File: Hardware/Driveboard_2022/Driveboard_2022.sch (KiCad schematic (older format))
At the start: 60 parts, among them SW1 SW_Push, SW2 SW_Push, SW3 SW_Push, SW4 SW_SPST, SW5 SW_Push, SW6 SW_Push, SW7 SW_Push, U1 OKI 3V3, U2 Teensy4.1_DEV-16771

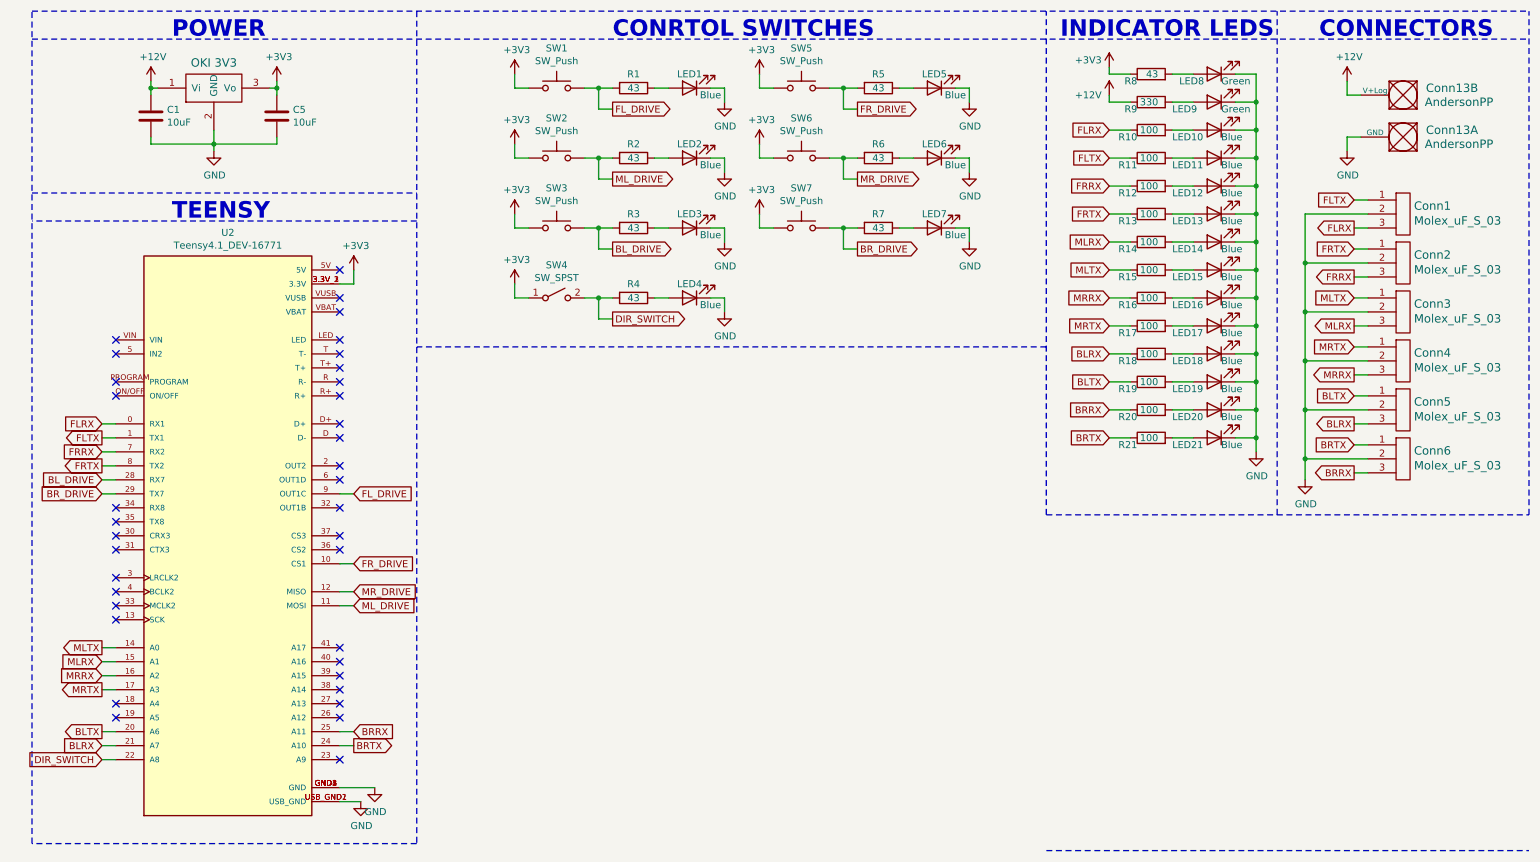
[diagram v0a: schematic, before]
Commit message: Fixed Ethernet Port
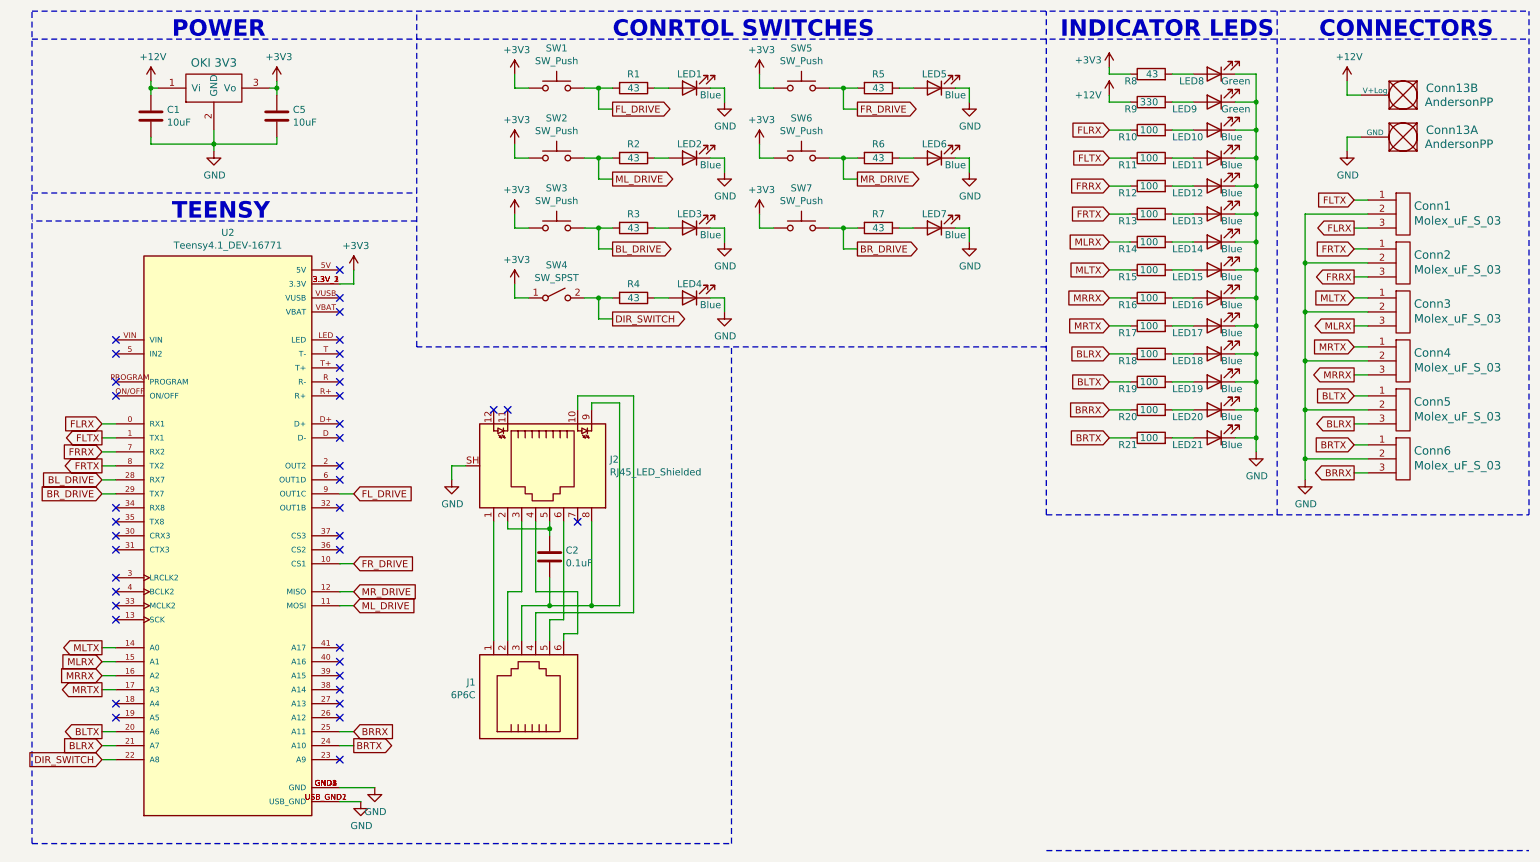
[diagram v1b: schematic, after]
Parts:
- added C2: 0.1uF, Capacitor_SMD:C_0603_1608Metric_Pad1.08x0.95mm_HandSolder, symbol Device:C
- added J1: 6P6C, Connector_PinHeader_2.00mm:PinHeader_2x03_P2.00mm_Vertical, symbol Connector:6P6C
- added J2: RJ45_LED_Shielded, MRDT_Connectors:RJ45_Teensy, symbol Connector:RJ45_LED_Shielded
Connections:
- net GND: now also J2.SH
- new net: J1.1, J2.1
- new net: J1.4, J2.10
- new net: C2.1, J2.2, J2.5
- new net: J1.2, J2.3
- new net: J1.6, J2.4
- new net: J1.5, J2.6
- new net: C2.2, J1.3, J2.8, J2.9
- no-connect marks 36 -> 39
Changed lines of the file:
@@
 CONNECTORS
-Wire Notes Line
-	3250 500  3250 6450
 Wire Notes Line
 	500  6450 500  500
@@
 Wire Notes Line
 	3250 2000 500  2000
-Wire Notes Line
-	3250 6450 500  6450
 $Comp
 L power:GND #PWR020
@@
 NoConn ~ 1100 5450
 NoConn ~ 1100 5550
+$Comp
+L Connector:6P6C J1
+U 1 1 62137B17
+P 4000 5400
+F 0 "J1" V 4103 5070 50  0000 R CNN
+F 1 "6P6C" V 4012 5070 50  0000 R CNN
+F 2 "Connector_PinHeader_2.00mm:PinHeader_2x03_P2.00mm_Vertical" V 4000 5425 50  0001 C CNN
+F 3 "~" V 4000 5425 50  0001 C CNN
+	1    4000 5400
+	0    1    -1   0
+$EndComp
+$Comp
+L power:GND #PWR02
+U 1 1 62152008
+P 3500 3850
+F 0 "#PWR02" H 3500 3600 50  0001 C CNN
+F 1 "GND" H 3505 3677 50  0000 C CNN
+F 2 "" H 3500 3850 50  0001 C CNN
+F 3 "" H 3500 3850 50  0001 C CNN
+	1    3500 3850
+	1    0    0    -1
+$EndComp
+Wire Wire Line
+	3500 3850 3500 3750
+Wire Wire Line
+	3500 3750 3600 3750
+Wire Wire Line
+	4200 4250 4200 4200
+Wire Wire Line
+	4200 4200 3900 4200
+Wire Wire Line
+	3900 4200 3900 4150
+Connection ~ 4200 4200
+Wire Wire Line
+	4200 4200 4200 4150
+Wire Wire Line
+	4200 4550 4200 4750
+Wire Wire Line
+	4500 4150 4500 4750
+Wire Wire Line
+	4500 4750 4200 4750
+Wire Wire Line
+	4500 3350 4500 3300
+Wire Wire Line
+	4500 3300 4700 3300
+Wire Wire Line
+	4400 3350 4400 3250
+Wire Wire Line
+	4400 3250 4800 3250
+NoConn ~ 3800 3350
+NoConn ~ 3900 3350
+Wire Wire Line
+	3800 4150 3800 5000
+Wire Wire Line
+	4000 5000 4000 4750
+Wire Wire Line
+	4000 4750 4200 4750
+Connection ~ 4200 4750
+Wire Wire Line
+	4300 5000 4300 4950
+Wire Wire Line
+	4300 4950 4400 4950
+Wire Wire Line
+	4400 4950 4400 4650
+Wire Wire Line
+	4400 4650 4100 4650
+Wire Wire Line
+	4100 4650 4100 4150
+Wire Wire Line
+	4200 4850 4300 4850
+Wire Wire Line
+	4300 4850 4300 4150
+Wire Wire Line
+	4200 4850 4200 5000
+Wire Wire Line
+	4100 5000 4100 4800
+Wire Wire Line
+	4100 4800 4800 4800
+Wire Wire Line
+	4800 3250 4800 4800
+Wire Wire Line
+	4700 4750 4500 4750
+Wire Wire Line
+	4700 3300 4700 4750
+Connection ~ 4500 4750
+Wire Wire Line
+	3900 5000 3900 4650
+Wire Wire Line
+	3900 4650 4000 4650
+Wire Wire Line
+	4000 4650 4000 4150
+NoConn ~ 4400 4150
+$Comp
+L Connector:RJ45_LED_Shielded J2
+U 1 1 62134E16
+P 4100 3750
+F 0 "J2" V 4054 4280 50  0000 L CNN
+F 1 "RJ45_LED_Shielded" V 4145 4280 50  0000 L CNN
+F 2 "MRDT_Connectors:RJ45_Teensy" V 4100 3775 50  0001 C CNN
+F 3 "~" V 4100 3775 50  0001 C CNN
+	1    4100 3750
+	0    1    1    0
+$EndComp
+$Comp
+L Device:C C2
+U 1 1 621516A0
+P 4200 4400
+F 0 "C2" H 4315 4446 50  0000 L CNN
+F 1 "0.1uF" H 4315 4355 50  0000 L CNN
+F 2 "Capacitor_SMD:C_0603_1608Metric_Pad1.08x0.95mm_HandSolder" H 4238 4250 50  0001 C CNN
+F 3 "~" H 4200 4400 50  0001 C CNN
+	1    4200 4400
+	1    0    0    -1
+$EndComp
+Wire Notes Line
+	3250 2900 3250 500
+Wire Notes Line
+	5500 6450 5500 2900
+Wire Notes Line
+	500  6450 5500 6450
 $EndSCHEMATC

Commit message: Board Review Changes
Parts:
- R1, R2, R3, R4, R5, R6, R7, R8: value 43 -> 100
- R9: value 330 -> 1k
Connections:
- net DIR_SWITCH: now also U2.33 (MCLK2); no longer U2.22 (A8)
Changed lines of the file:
@@
 Wire Wire Line
 	1000 3850 1100 3850
-Text GLabel 1000 5850 0    50   Input ~ 0
+Text GLabel 1000 4750 0    50   Input ~ 0
 DIR_SWITCH
 Wire Wire Line
-	1000 5850 1100 5850
+	1000 4750 1100 4750
 $Comp
 L power:+12V #PWR01
@@
 P 4800 1050
 F 0 "R1" V 4700 1050 50  0000 C CNN
-F 1 "43" V 4800 1050 50  0000 C CNN
+F 1 "100" V 4800 1050 50  0000 C CNN
 F 2 "Resistor_SMD:R_0603_1608Metric_Pad0.98x0.95mm_HandSolder" V 4730 1050 50  0001 C CNN
 F 3 "~" H 4800 1050 50  0001 C CNN
@@
 P 4800 1550
 F 0 "R2" V 4700 1550 50  0000 C CNN
-F 1 "43" V 4800 1550 50  0000 C CNN
+F 1 "100" V 4800 1550 50  0000 C CNN
 F 2 "Resistor_SMD:R_0603_1608Metric_Pad0.98x0.95mm_HandSolder" V 4730 1550 50  0001 C CNN
 F 3 "~" H 4800 1550 50  0001 C CNN
@@
 P 4800 2050
 F 0 "R3" V 4700 2050 50  0000 C CNN
-F 1 "43" V 4800 2050 50  0000 C CNN
+F 1 "100" V 4800 2050 50  0000 C CNN
 F 2 "Resistor_SMD:R_0603_1608Metric_Pad0.98x0.95mm_HandSolder" V 4730 2050 50  0001 C CNN
 F 3 "~" H 4800 2050 50  0001 C CNN
@@
 P 6550 1050
 F 0 "R5" V 6450 1050 50  0000 C CNN
-F 1 "43" V 6550 1050 50  0000 C CNN
+F 1 "100" V 6550 1050 50  0000 C CNN
 F 2 "Resistor_SMD:R_0603_1608Metric_Pad0.98x0.95mm_HandSolder" V 6480 1050 50  0001 C CNN
 F 3 "~" H 6550 1050 50  0001 C CNN
@@
 P 6550 1550
 F 0 "R6" V 6450 1550 50  0000 C CNN
-F 1 "43" V 6550 1550 50  0000 C CNN
+F 1 "100" V 6550 1550 50  0000 C CNN
 F 2 "Resistor_SMD:R_0603_1608Metric_Pad0.98x0.95mm_HandSolder" V 6480 1550 50  0001 C CNN
 F 3 "~" H 6550 1550 50  0001 C CNN
@@
 P 6550 2050
 F 0 "R7" V 6450 2050 50  0000 C CNN
-F 1 "43" V 6550 2050 50  0000 C CNN
+F 1 "100" V 6550 2050 50  0000 C CNN
 F 2 "Resistor_SMD:R_0603_1608Metric_Pad0.98x0.95mm_HandSolder" V 6480 2050 50  0001 C CNN
 F 3 "~" H 6550 2050 50  0001 C CNN
@@
 P 4800 2550
 F 0 "R4" V 4700 2550 50  0000 C CNN
-F 1 "43" V 4800 2550 50  0000 C CNN
+F 1 "100" V 4800 2550 50  0000 C CNN
 F 2 "Resistor_SMD:R_0603_1608Metric_Pad0.98x0.95mm_HandSolder" V 4730 2550 50  0001 C CNN
 F 3 "~" H 4800 2550 50  0001 C CNN
@@
 P 8500 950
 F 0 "R8" V 8450 1050 50  0000 L CNN
-F 1 "43" V 8500 900 50  0000 L CNN
+F 1 "100" V 8500 900 50  0000 L CNN
 F 2 "Resistor_SMD:R_0603_1608Metric_Pad0.98x0.95mm_HandSolder" V 8430 950 50  0001 C CNN
 F 3 "~" H 8500 950 50  0001 C CNN
@@
 P 8500 1150
 F 0 "R9" V 8450 1250 50  0000 L CNN
-F 1 "330" V 8500 1100 50  0000 L CNN
+F 1 "1k" V 8500 1100 50  0000 L CNN
 F 2 "Resistor_SMD:R_0603_1608Metric_Pad0.98x0.95mm_HandSolder" V 8430 1150 50  0001 C CNN
 F 3 "~" H 8500 1150 50  0001 C CNN
@@
 NoConn ~ 2700 5850
 NoConn ~ 1100 4850
-NoConn ~ 1100 4750
 NoConn ~ 1100 4650
 NoConn ~ 1100 4550
@@
 Wire Notes Line
 	500  6450 5500 6450
+NoConn ~ 1100 5850
 $EndSCHEMATC

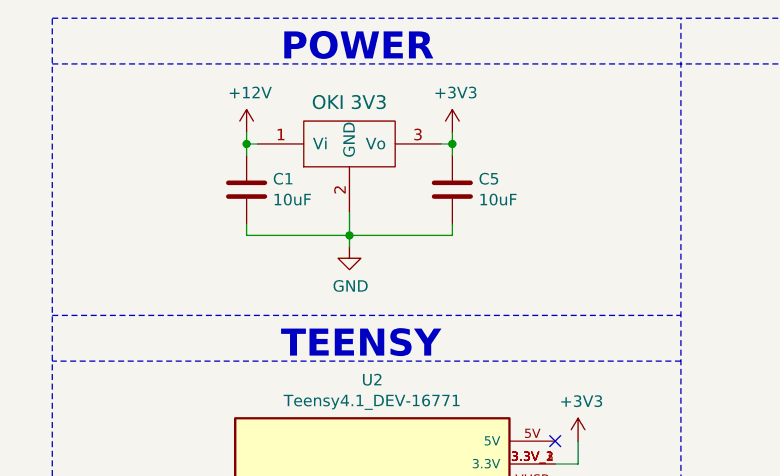
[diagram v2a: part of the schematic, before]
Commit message: Changed Buck Converter; Redid Gerbs
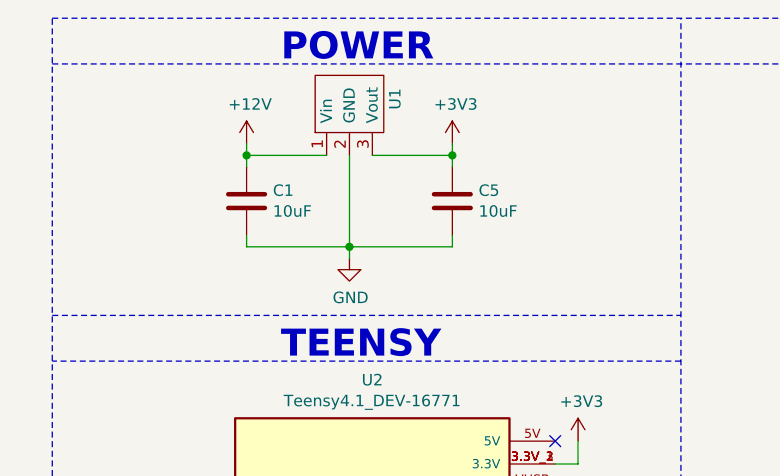
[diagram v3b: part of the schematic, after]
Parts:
- removed U1: OKI 3V3, MRDT_Devices:OKI_Horizontal, symbol MRDT_Devices:OKI
- added U1: TSR1-2433, MRDT_Devices:TSR_1-2433, symbol MRDT_Devices:TSR1-2433
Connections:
- net +12V: now also U1.1 (Vin)
- net +3V3: now also U1.3 (Vout)
- net GND: now also U1.2 (GND)
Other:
- moved on the sheet: C1, C5
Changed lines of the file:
@@
 L power:GND #PWR05
 U 1 1 614AB02E
-P 1800 1500
-F 0 "#PWR05" H 1800 1250 50  0001 C CNN
-F 1 "GND" H 1805 1327 50  0000 C CNN
-F 2 "" H 1800 1500 50  0001 C CNN
-F 3 "" H 1800 1500 50  0001 C CNN
-	1    1800 1500
+P 1800 1550
+F 0 "#PWR05" H 1800 1300 50  0001 C CNN
+F 1 "GND" H 1805 1377 50  0000 C CNN
+F 2 "" H 1800 1550 50  0001 C CNN
+F 3 "" H 1800 1550 50  0001 C CNN
+	1    1800 1550
 	1    0    0    -1
 $EndComp
@@
 L Device:C C1
 U 1 1 614B147D
-P 1350 1250
-F 0 "C1" H 1465 1296 50  0000 L CNN
-F 1 "10uF" H 1465 1205 50  0000 L CNN
-F 2 "Capacitor_SMD:C_0603_1608Metric_Pad1.08x0.95mm_HandSolder" H 1388 1100 50  0001 C CNN
-F 3 "~" H 1350 1250 50  0001 C CNN
-	1    1350 1250
+P 1350 1300
+F 0 "C1" H 1465 1346 50  0000 L CNN
+F 1 "10uF" H 1465 1255 50  0000 L CNN
+F 2 "Capacitor_SMD:C_0603_1608Metric_Pad1.08x0.95mm_HandSolder" H 1388 1150 50  0001 C CNN
+F 3 "~" H 1350 1300 50  0001 C CNN
+	1    1350 1300
 	1    0    0    -1
 $EndComp
@@
 L Device:C C5
 U 1 1 614B3AC0
-P 2250 1250
-F 0 "C5" H 2365 1296 50  0000 L CNN
-F 1 "10uF" H 2365 1205 50  0000 L CNN
-F 2 "Capacitor_SMD:C_0603_1608Metric_Pad1.08x0.95mm_HandSolder" H 2288 1100 50  0001 C CNN
-F 3 "~" H 2250 1250 50  0001 C CNN
-	1    2250 1250
+P 2250 1300
+F 0 "C5" H 2365 1346 50  0000 L CNN
+F 1 "10uF" H 2365 1255 50  0000 L CNN
+F 2 "Capacitor_SMD:C_0603_1608Metric_Pad1.08x0.95mm_HandSolder" H 2288 1150 50  0001 C CNN
+F 3 "~" H 2250 1300 50  0001 C CNN
+	1    2250 1300
 	1    0    0    -1
 $EndComp
@@
 L power:+3V3 #PWR09
 U 1 1 614B46E4
-P 2250 1000
-F 0 "#PWR09" H 2250 850 50  0001 C CNN
-F 1 "+3V3" H 2265 1173 50  0000 C CNN
-F 2 "" H 2250 1000 50  0001 C CNN
-F 3 "" H 2250 1000 50  0001 C CNN
-	1    2250 1000
+P 2250 1050
+F 0 "#PWR09" H 2250 900 50  0001 C CNN
+F 1 "+3V3" H 2265 1223 50  0000 C CNN
+F 2 "" H 2250 1050 50  0001 C CNN
+F 3 "" H 2250 1050 50  0001 C CNN
+	1    2250 1050
 	1    0    0    -1
 $EndComp
@@
 L power:+12V #PWR01
 U 1 1 618F1463
-P 1350 1000
-F 0 "#PWR01" H 1350 850 50  0001 C CNN
-F 1 "+12V" H 1365 1173 50  0000 C CNN
-F 2 "" H 1350 1000 50  0001 C CNN
-F 3 "" H 1350 1000 50  0001 C CNN
-	1    1350 1000
+P 1350 1050
+F 0 "#PWR01" H 1350 900 50  0001 C CNN
+F 1 "+12V" H 1365 1223 50  0000 C CNN
+F 2 "" H 1350 1050 50  0001 C CNN
+F 3 "" H 1350 1050 50  0001 C CNN
+	1    1350 1050
 	1    0    0    -1
 $EndComp
@@
 	9250 3350 9250 3550
 Wire Wire Line
-	1350 1000 1350 1050
-Wire Wire Line
-	1400 1050 1350 1050
-Connection ~ 1350 1050
-Wire Wire Line
 	1350 1050 1350 1100
-Wire Wire Line
-	2250 1000 2250 1050
-Wire Wire Line
-	2200 1050 2250 1050
-Connection ~ 2250 1050
+Connection ~ 1350 1100
+Wire Wire Line
+	1350 1100 1350 1150
 Wire Wire Line
 	2250 1050 2250 1100
-Wire Wire Line
-	2250 1400 2250 1450
-Wire Wire Line
-	2250 1450 1800 1450
-Wire Wire Line
-	1350 1450 1350 1400
-Wire Wire Line
-	1800 1350 1800 1450
-Connection ~ 1800 1450
-Wire Wire Line
-	1800 1450 1350 1450
-Wire Wire Line
-	1800 1500 1800 1450
+Connection ~ 2250 1100
+Wire Wire Line
+	2250 1100 2250 1150
+Wire Wire Line
+	2250 1450 2250 1500
+Wire Wire Line
+	2250 1500 1800 1500
+Wire Wire Line
+	1350 1500 1350 1450
+Connection ~ 1800 1500
+Wire Wire Line
+	1800 1500 1350 1500
+Wire Wire Line
+	1800 1550 1800 1500
 Wire Wire Line
 	1000 5650 1100 5650
@@
 Wire Notes Line
 	7750 4100 7750 500
-$Comp
-L MRDT_Devices:OKI U1
-U 1 1 62597FF4
-P 1600 1150
-F 0 "U1" H 1650 1100 60  0001 C CNN
-F 1 "OKI 3V3" H 1800 1431 60  0000 C CNN
-F 2 "MRDT_Devices:OKI_Horizontal" H 1400 1050 60  0001 C CNN
-F 3 "" H 1400 1050 60  0001 C CNN
-	1    1600 1150
-	1    0    0    -1
-$EndComp
 NoConn ~ 2700 2350
 NoConn ~ 2700 2550
@@
 	500  6450 5500 6450
 NoConn ~ 1100 5850
+$Comp
+L MRDT_Devices:TSR1-2433 U1
+U 1 1 622A4B32
+P 1800 1100
+F 0 "U1" H 2000 900 50  0000 L CNN
+F 1 "TSR1-2433" V 2200 1100 50  0001 C CNN
+F 2 "MRDT_Devices:TSR_1-2433" H 2100 1200 50  0001 C CNN
+F 3 "" H 2100 1200 50  0001 C CNN
+	1    1800 1100
+	0    -1   -1   0
+$EndComp
+Wire Wire Line
+	1800 1100 1800 1500
+Wire Wire Line
+	1900 1100 2250 1100
+Wire Wire Line
+	1350 1100 1700 1100
 $EndSCHEMATC
